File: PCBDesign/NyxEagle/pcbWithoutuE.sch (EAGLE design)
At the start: 17 parts, among them IC1 DRV8304SRHAR

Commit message: Update pcbWithoutuE.brd and pcbWithoutuE.sch
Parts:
- added IN, IN1, JP1, SPI: (no value), jumper:JP4E
- R1, R2: value 10k -> 5.1k
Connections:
- new net CAL: IC1.CAL, JP1.1
- new net ENABLE: IC1.ENABLE, JP1.2
- new net INHA: IC1.INHA, IN.1
- new net INHB: IC1.INHB, IN.3
- new net INHC: IC1.INHC, IN1.1
- new net INLA: IC1.INLA, IN.2
- new net INLB: IC1.INLB, IN.4
- new net INLC: IC1.INLC, IN1.2
- new net N$6: IN1.3
- new net N$7: JP1.4
- new net N$8: IN1.4
- new net NSCS: IC1.NSCS, SPI.1
- new net SCLK: IC1.SCLK, SPI.2
- new net SDI: IC1.SDI, SPI.3
- net NFAULT: now also JP1.3
- net SDO: now also SPI.4

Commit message: Update pcbWithoutuE.brd and pcbWithoutuE.sch
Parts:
- added ADCO: (no value), jumper:JP4E
- added INPUT, OUT1, OUT2, OUT3: (no value), wirepad:SMD2
- added R3, R4, R5: (no value), resistor_mod:R-EU_
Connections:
- new net N$10: ADCO.4
- new net SNA: IC1.SNA, R3.1
- new net SNB: IC1.SNB, R4.1
- new net SNC: IC1.SNC, R5.1
- new net SOA: ADCO.1, IC1.SOA
- new net SOB: ADCO.2, IC1.SOB
- new net SOC: ADCO.3, IC1.SOC
- new net SPA: IC1.SPA, R3.2, U$2.S
- new net SPB: IC1.SPB, R4.2, U$4.S
- new net SPC: IC1.SPC, R5.2, U$6.S
- net +3V3: now also IC1.DVDD
- net SHA: now also OUT1.P
- net SHB: now also OUT2.P
- net SHC: now also OUT3.P
- net VM: now also INPUT.P

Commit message: Update pcbWithoutuE.brd and pcbWithoutuE.sch
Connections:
- removed net NFAULT\: R1.1
- net NFAULT: now also R1.1
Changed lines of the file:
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@@
-</segment>
-</net>
-<net name="NFAULT\" class="0">
-<segment>
-<pinref part="R1" gate="G$1" pin="1"/>
-<wire x1="53.34" y1="99.06" x2="43.18" y2="99.06" width="0.1524" layer="91"/>
-<label x="43.18" y="96.52" size="1.778" layer="95"/>
 </segment>
 </net>
@@
 <label x="-10.16" y="101.6" size="1.778" layer="95" rot="R90"/>
 </segment>
+<segment>
+<pinref part="R1" gate="G$1" pin="1"/>
+<wire x1="53.34" y1="99.06" x2="43.18" y2="99.06" width="0.1524" layer="91"/>
+<label x="43.18" y="96.52" size="1.778" layer="95"/>
+</segment>
 </net>

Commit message: Update pcbWithoutuE.brd and pcbWithoutuE.sch
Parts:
- added GND: (no value), wirepad:SMD2
- added R10, R9: (no value), rcl:R-EU_R0201
- added R6, R7: 0, rcl:R-EU_R0805W
- added R8: 0, rcl:R-EU_R0201
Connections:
- new net AGND: C3.-, C4.2, C6.2, C7.2, C8.2, GND.P, R10.1, R3.1, R4.1, R5.1, R6.1, R7.1, R8.1, R9.1
- net GND: now also R6.2, R7.2; no longer C3.-, C4.2, C6.2, C7.2, C8.2
- net SNA: now also R8.2; no longer R3.1
- net SNB: now also R9.2; no longer R4.1
- net SNC: now also R10.2; no longer R5.1

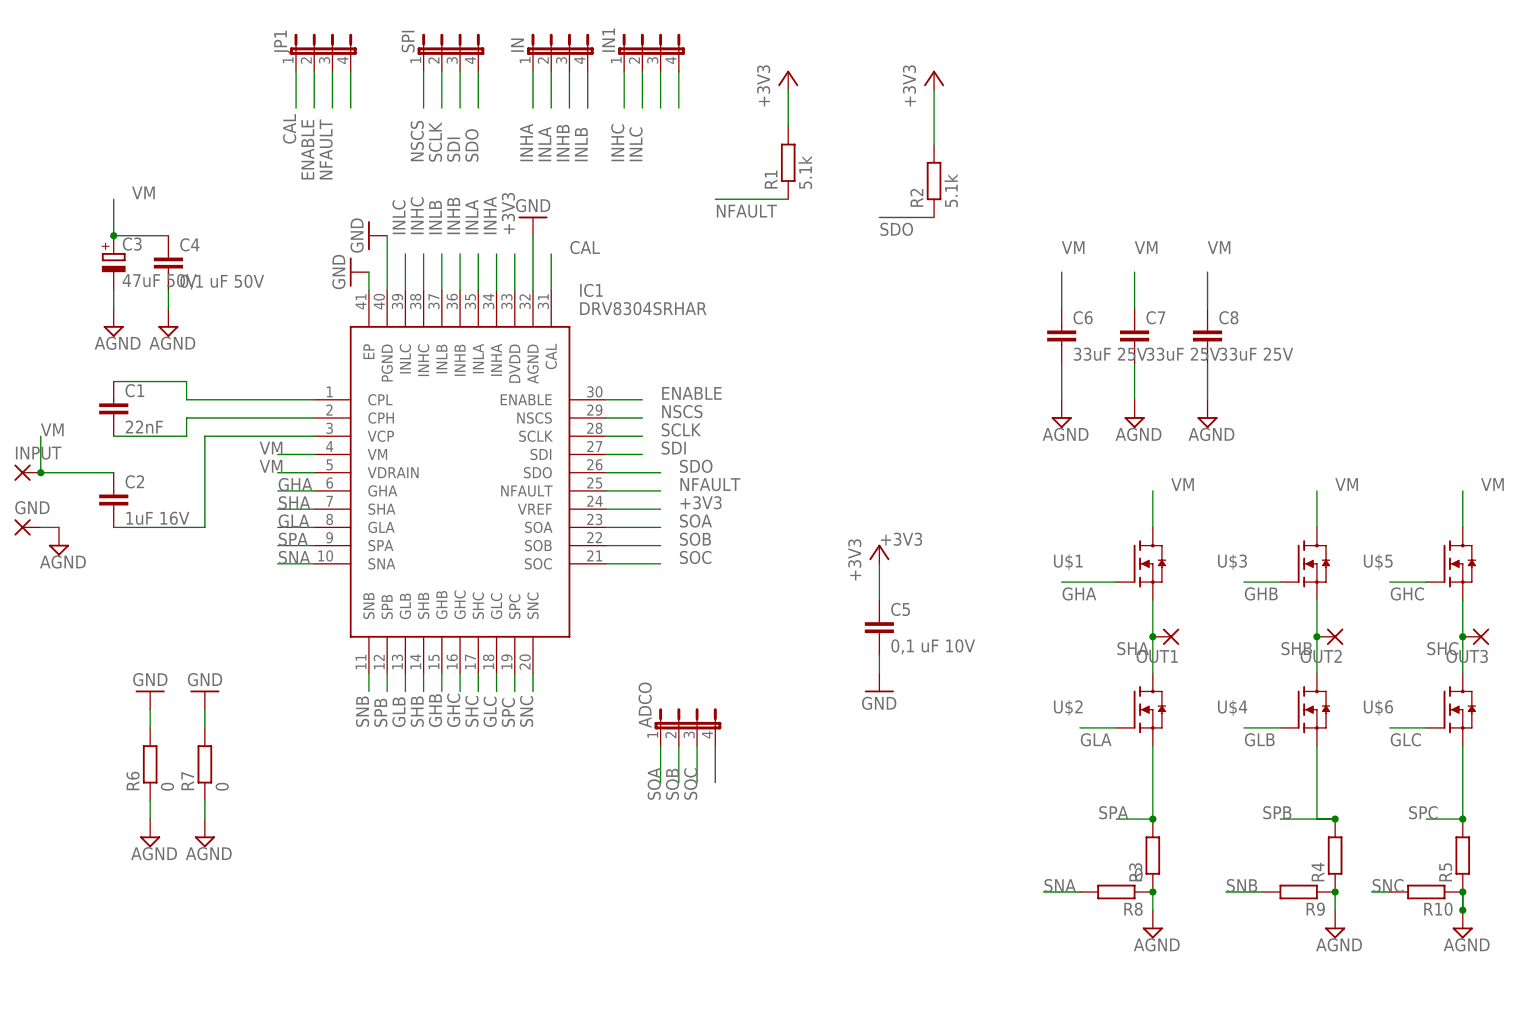
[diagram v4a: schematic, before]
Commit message: Change of shunt resistors to smaller.
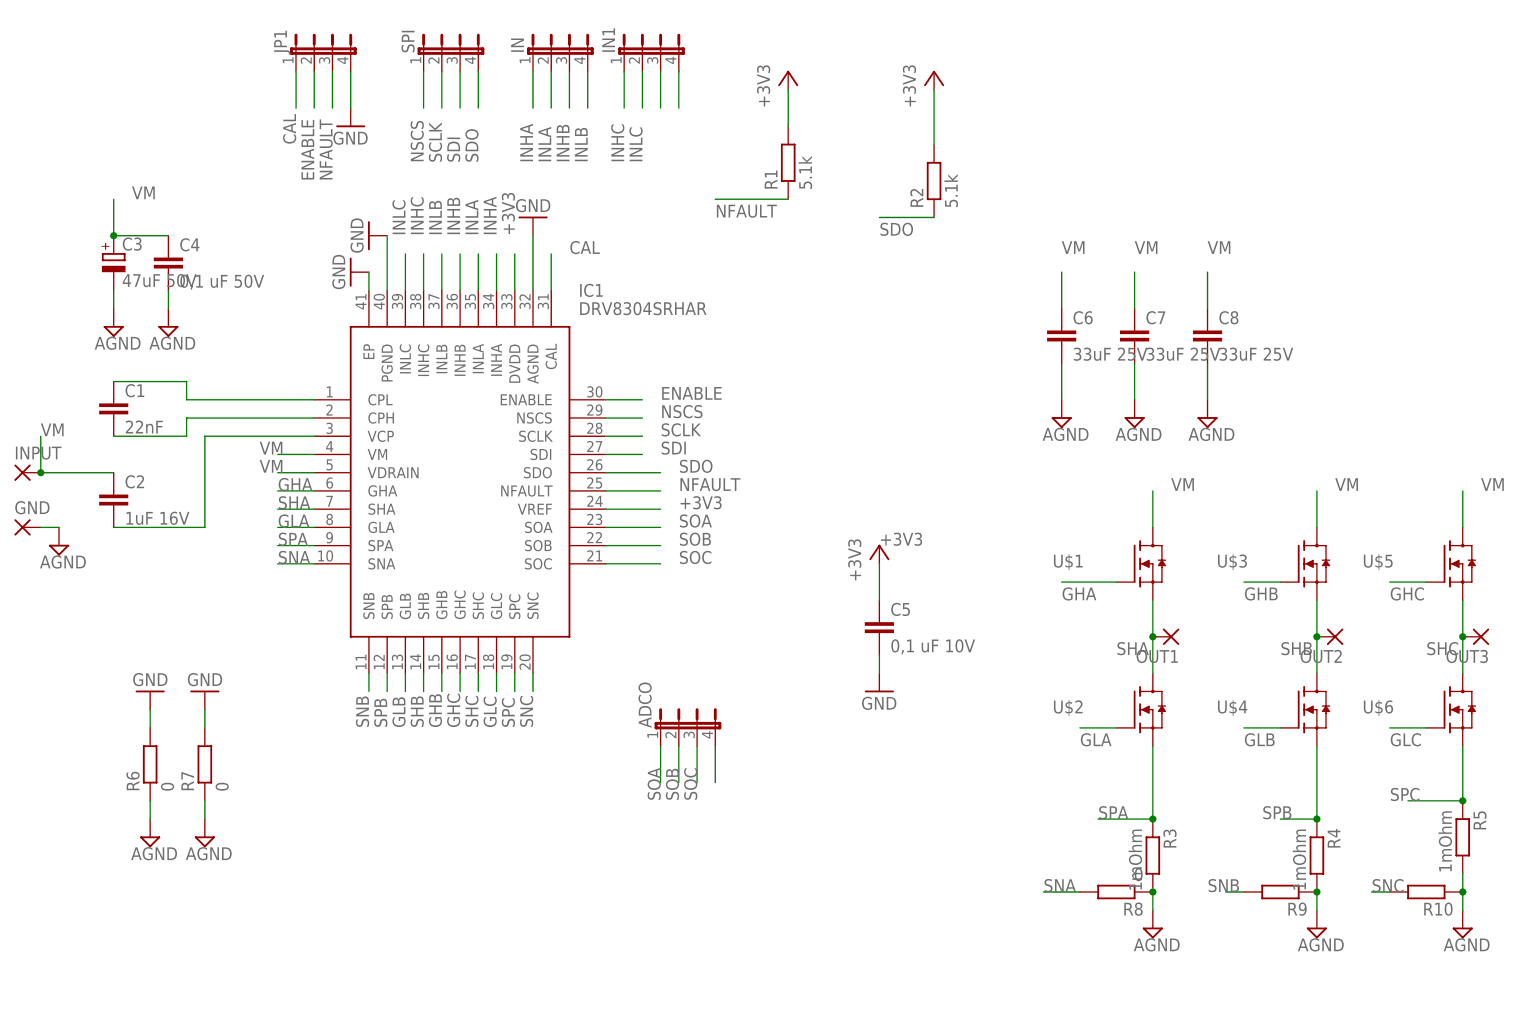
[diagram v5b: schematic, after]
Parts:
- R3, R4, R5: value (none) -> 1mOhm; device resistor_mod:R-EU_ -> resistor_mod:R-EU_R1216_SHUNT
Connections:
- removed net N$7: JP1.4
- net AGND: now also R3.2, R4.2, R5.2; no longer R3.1, R4.1, R5.1
- net GND: now also JP1.4
- net SPA: now also R3.1; no longer R3.2
- net SPB: now also R4.1; no longer R4.2
- net SPC: now also R5.1; no longer R5.2
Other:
- moved on the sheet: R3, R4, R5, R9
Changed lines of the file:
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@@
 <layer number="97" name="Info" color="7" fill="1" visible="yes" active="yes"/>
 <layer number="98" name="Guide" color="6" fill="1" visible="yes" active="yes"/>
+<layer number="99" name="SpiceOrder" color="5" fill="1" visible="yes" active="yes"/>
 </layers>
 <schematic xreflabel="%F%N/%S.%C%R" xrefpart="/%S.%C%R">
@@
 <part name="IN" library="jumper" library_urn="urn:adsk.eagle:library:252" deviceset="JP4E" device="" package3d_urn="urn:adsk.eagle:package:15463/1"/>
 <part name="IN1" library="jumper" library_urn="urn:adsk.eagle:library:252" deviceset="JP4E" device="" package3d_urn="urn:adsk.eagle:package:15463/1"/>
-<part name="R3" library="resistor_mod" deviceset="R-EU_" device=""/>
-<part name="R4" library="resistor_mod" deviceset="R-EU_" device=""/>
-<part name="R5" library="resistor_mod" deviceset="R-EU_" device=""/>
+<part name="R3" library="resistor_mod" deviceset="R-EU_" device="R1216_SHUNT" value="1mOhm"/>
+<part name="R4" library="resistor_mod" deviceset="R-EU_" device="R1216_SHUNT" value="1mOhm"/>
+<part name="R5" library="resistor_mod" deviceset="R-EU_" device="R1216_SHUNT" value="1mOhm"/>
 <part name="ADCO" library="jumper" library_urn="urn:adsk.eagle:library:252" deviceset="JP4E" device="" package3d_urn="urn:adsk.eagle:package:15463/1"/>
 <part name="OUT1" library="wirepad" library_urn="urn:adsk.eagle:library:412" deviceset="SMD2" device="" package3d_urn="urn:adsk.eagle:package:30839/1"/>
@@
 <part name="R9" library="rcl" library_urn="urn:adsk.eagle:library:334" deviceset="R-EU_" device="R0201" package3d_urn="urn:adsk.eagle:package:23593/1"/>
 <part name="R10" library="rcl" library_urn="urn:adsk.eagle:library:334" deviceset="R-EU_" device="R0201" package3d_urn="urn:adsk.eagle:package:23593/1"/>
+<part name="GND7" library="supply1" library_urn="urn:adsk.eagle:library:371" deviceset="GND" device=""/>
 </parts>
 <sheets>
@@
 <instance part="IN" gate="G$1" x="20.32" y="119.38"/>
 <instance part="IN1" gate="G$1" x="33.02" y="119.38"/>
-<instance part="R3" gate="G$1" x="104.14" y="7.62" rot="R90"/>
-<instance part="R4" gate="G$1" x="129.54" y="7.62" rot="R90"/>
-<instance part="R5" gate="G$1" x="147.32" y="7.62" rot="R90"/>
+<instance part="R3" gate="G$1" x="104.14" y="7.62" rot="R270"/>
+<instance part="R4" gate="G$1" x="127" y="7.62" rot="R270"/>
+<instance part="R5" gate="G$1" x="147.32" y="10.16" rot="R270"/>
 <instance part="ADCO" gate="G$1" x="38.1" y="25.4"/>
 <instance part="OUT1" gate="1" x="106.68" y="38.1" rot="R180"/>
@@
 <instance part="SUPPLY7" gate="G$1" x="101.6" y="68.58"/>
 <instance part="SUPPLY8" gate="G$1" x="104.14" y="-2.54"/>
-<instance part="SUPPLY9" gate="G$1" x="129.54" y="-2.54"/>
+<instance part="SUPPLY9" gate="G$1" x="127" y="-2.54"/>
 <instance part="R6" gate="G$1" x="-35.56" y="20.32" rot="R90"/>
 <instance part="R7" gate="G$1" x="-27.94" y="20.32" rot="R90"/>
@@
 <instance part="GND2" gate="1" x="-27.94" y="30.48" rot="R180"/>
 <instance part="R8" gate="G$1" x="99.06" y="2.54" rot="R180"/>
-<instance part="R9" gate="G$1" x="124.46" y="2.54" rot="R180"/>
+<instance part="R9" gate="G$1" x="121.92" y="2.54" rot="R180"/>
 <instance part="R10" gate="G$1" x="142.24" y="2.54" rot="R180"/>
+<instance part="GND7" gate="1" x="-7.62" y="109.22"/>
 </instances>
 <busses>
@@
 <pinref part="GND2" gate="1" pin="GND"/>
 <wire x1="-27.94" y1="27.94" x2="-27.94" y2="25.4" width="0.1524" layer="91"/>
+</segment>
+<segment>
+<pinref part="JP1" gate="G$1" pin="4"/>
+<wire x1="-7.62" y1="116.84" x2="-7.62" y2="111.76" width="0.1524" layer="91"/>
+<pinref part="GND7" gate="1" pin="GND"/>
 </segment>
 </net>
@@
 </segment>
 </net>
-<net name="N$7" class="0">
-<segment>
-<pinref part="JP1" gate="G$1" pin="4"/>
-<wire x1="-7.62" y1="116.84" x2="-7.62" y2="111.76" width="0.1524" layer="91"/>
-</segment>
-</net>
 <net name="CAL" class="0">
 <segment>
@@
 </segment>
 <segment>
-<pinref part="R3" gate="G$1" pin="2"/>
+<pinref part="R3" gate="G$1" pin="1"/>
 <pinref part="U$2" gate="G$1" pin="S"/>
 <wire x1="104.14" y1="12.7" x2="104.14" y2="22.86" width="0.1524" layer="91"/>
-<wire x1="104.14" y1="12.7" x2="99.06" y2="12.7" width="0.1524" layer="91"/>
+<wire x1="104.14" y1="12.7" x2="96.52" y2="12.7" width="0.1524" layer="91"/>
 <junction x="104.14" y="12.7"/>
 <label x="96.52" y="12.7" size="1.778" layer="95"/>
@@
 <segment>
 <pinref part="R9" gate="G$1" pin="2"/>
-<wire x1="119.38" y1="2.54" x2="114.3" y2="2.54" width="0.1524" layer="91"/>
-<label x="114.3" y="2.54" size="1.778" layer="95"/>
+<wire x1="116.84" y1="2.54" x2="114.3" y2="2.54" width="0.1524" layer="91"/>
+<label x="111.76" y="2.54" size="1.778" layer="95"/>
 </segment>
 </net>
@@
 </segment>
 <segment>
-<pinref part="R4" gate="G$1" pin="2"/>
 <pinref part="U$4" gate="G$1" pin="S"/>
-<wire x1="129.54" y1="12.7" x2="127" y2="12.7" width="0.1524" layer="91"/>
 <wire x1="127" y1="12.7" x2="127" y2="22.86" width="0.1524" layer="91"/>
-<wire x1="129.54" y1="12.7" x2="121.92" y2="12.7" width="0.1524" layer="91"/>
-<junction x="129.54" y="12.7"/>
 <label x="119.38" y="12.7" size="1.778" layer="95"/>
+<pinref part="R4" gate="G$1" pin="1"/>
+<wire x1="127" y1="12.7" x2="121.92" y2="12.7" width="0.1524" layer="91"/>
+<junction x="127" y="12.7"/>
 </segment>
 </net>
@@
 </segment>
 <segment>
-<pinref part="R5" gate="G$1" pin="2"/>
+<pinref part="R5" gate="G$1" pin="1"/>
 <pinref part="U$6" gate="G$1" pin="S"/>
-<wire x1="147.32" y1="12.7" x2="147.32" y2="22.86" width="0.1524" layer="91"/>
-<wire x1="147.32" y1="12.7" x2="142.24" y2="12.7" width="0.1524" layer="91"/>
-<junction x="147.32" y="12.7"/>
-<label x="139.7" y="12.7" size="1.778" layer="95"/>
+<wire x1="147.32" y1="15.24" x2="147.32" y2="22.86" width="0.1524" layer="91"/>
+<wire x1="147.32" y1="15.24" x2="139.7" y2="15.24" width="0.1524" layer="91"/>
+<junction x="147.32" y="15.24"/>
+<label x="137.16" y="15.24" size="1.778" layer="95"/>
 </segment>
 </net>
@@
 </segment>
 <segment>
-<pinref part="R3" gate="G$1" pin="1"/>
+<pinref part="R8" gate="G$1" pin="1"/>
+<pinref part="R3" gate="G$1" pin="2"/>
+<pinref part="SUPPLY8" gate="G$1" pin="AGND"/>
 <wire x1="104.14" y1="0" x2="104.14" y2="2.54" width="0.1524" layer="91"/>
-<pinref part="SUPPLY8" gate="G$1" pin="AGND"/>
-<pinref part="R8" gate="G$1" pin="1"/>
 <junction x="104.14" y="2.54"/>
 </segment>
 <segment>
+<pinref part="R9" gate="G$1" pin="1"/>
+<pinref part="R4" gate="G$1" pin="2"/>
 <pinref part="SUPPLY9" gate="G$1" pin="AGND"/>
-<pinref part="R9" gate="G$1" pin="1"/>
-<wire x1="129.54" y1="2.54" x2="129.54" y2="0" width="0.1524" layer="91"/>
-<pinref part="R4" gate="G$1" pin="1"/>
-<junction x="129.54" y="2.54"/>
-</segment>
-<segment>
-<pinref part="R5" gate="G$1" pin="1"/>
+<wire x1="127" y1="0" x2="127" y2="2.54" width="0.1524" layer="91"/>
+<junction x="127" y="2.54"/>
+</segment>
+<segment>
 <pinref part="R10" gate="G$1" pin="1"/>
-<pinref part="SUPPLY5" gate="G$1" pin="AGND"/>
-<junction x="147.32" y="0"/>
+<pinref part="R5" gate="G$1" pin="2"/>
+<wire x1="147.32" y1="2.54" x2="147.32" y2="5.08" width="0.1524" layer="91"/>
 <pinref part="SUPPLY5" gate="G$1" pin="AGND"/>
 <wire x1="147.32" y1="0" x2="147.32" y2="2.54" width="0.1524" layer="91"/>
 <junction x="147.32" y="2.54"/>
-<wire x1="147.32" y1="0" x2="147.32" y2="2.54" width="0.1524" layer="91"/>
-</segment>
-</net>
+</segment>
+</net>
